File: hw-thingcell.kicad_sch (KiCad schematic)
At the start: 67 parts, among them J1 Conn_01x02_Pin, J2 Conn_Coaxial, J3 SIM8060-6-0-14-00-A, J4 Conn_01x08_Pin, K1 JRC-21F(4100), Q1 PMBT3904235, Q2 PMBT3904235, SW1 SW_Push, U1 ESP32-WROOM-32, U2 SIM800C, U3 NCP1117-3.3_SOT223

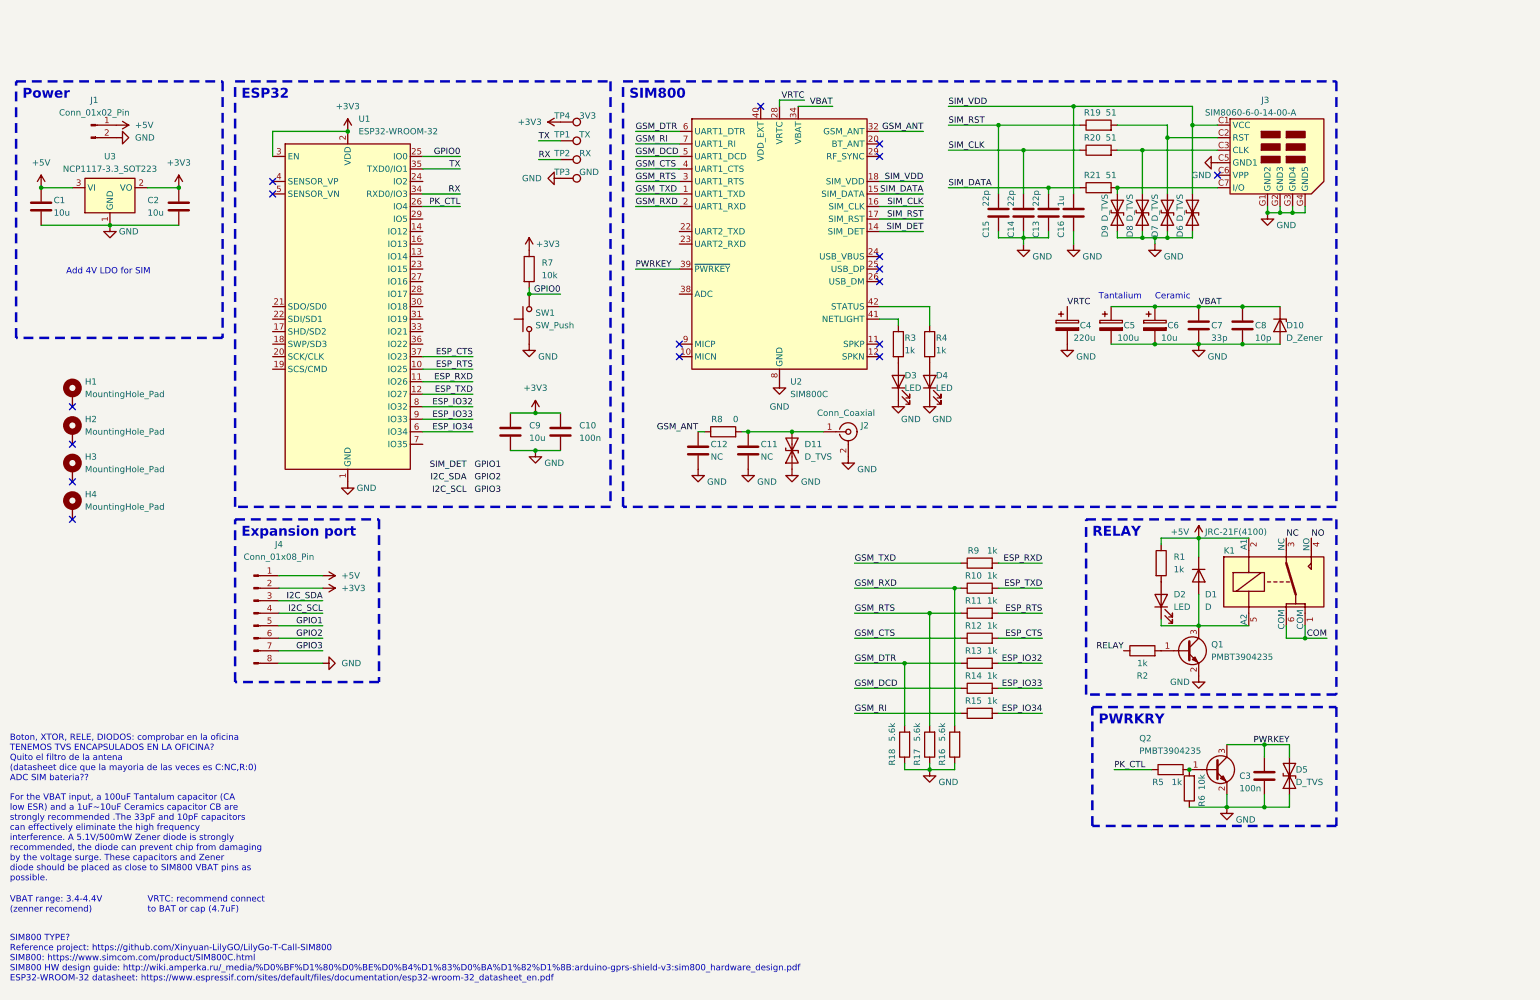
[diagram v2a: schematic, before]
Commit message: Replace SIM800C with SIM868
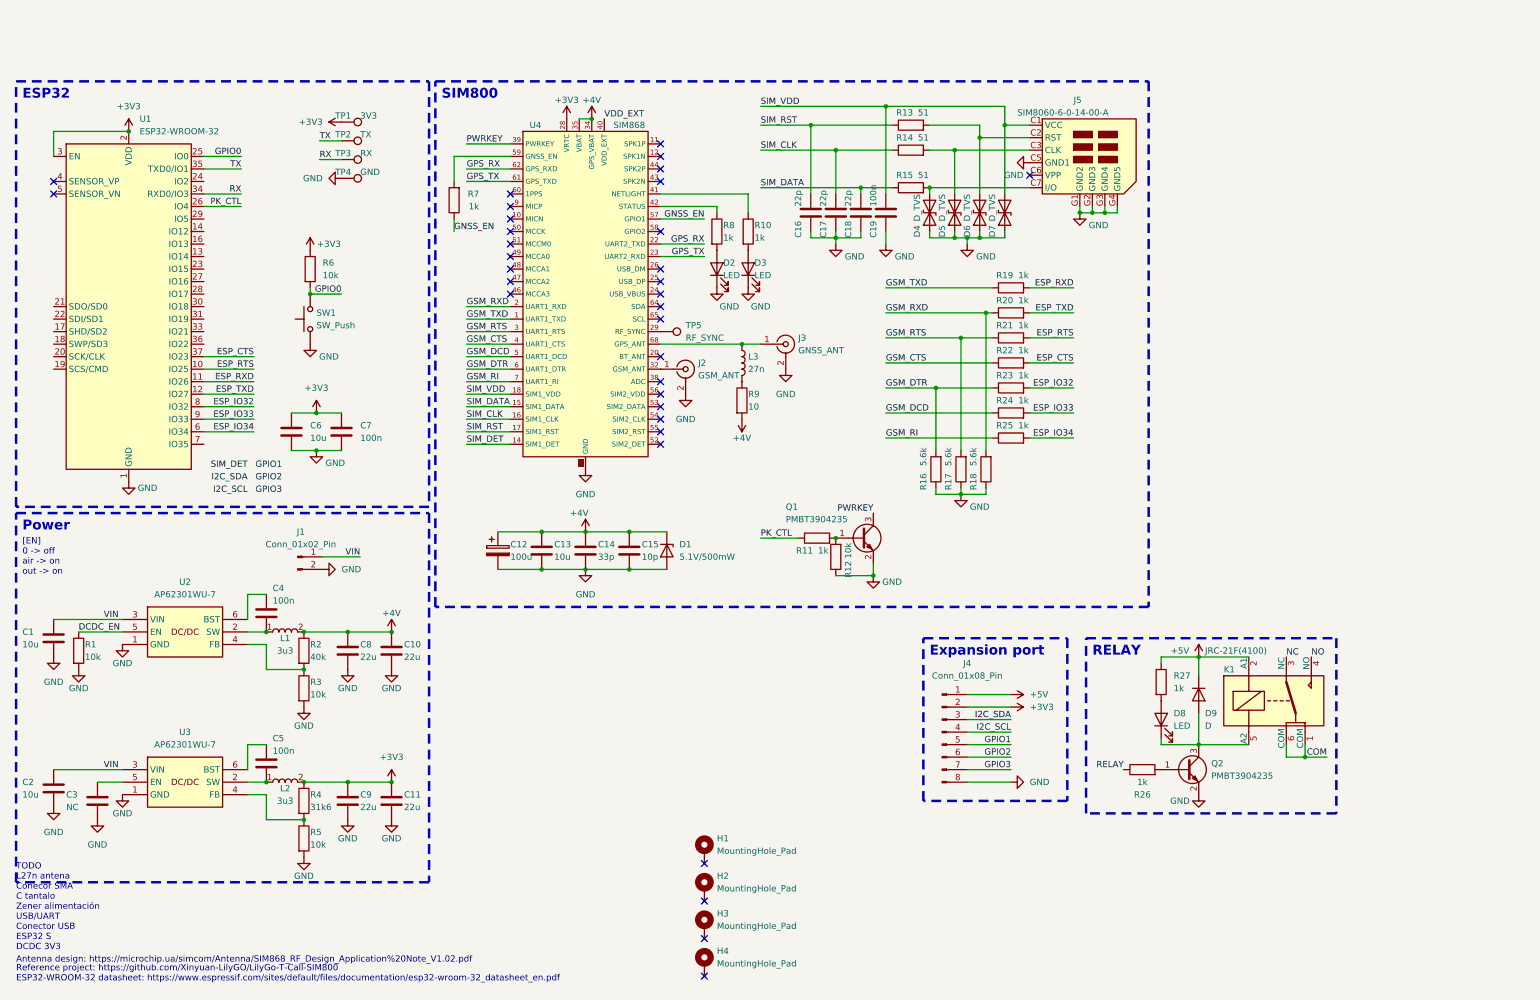
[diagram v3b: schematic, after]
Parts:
- removed C12: NC, Capacitor_SMD:C_0402_1005Metric, symbol Device:C
- removed C4: 220u, symbol Device:C_Polarized
- removed C5: 100u, symbol Device:C_Polarized
- removed C6: 10u, symbol Device:C_Polarized
- removed C7: 33p, Capacitor_SMD:C_0402_1005Metric, symbol Device:C
- removed D10: D_Zener, symbol Device:D_Zener
- removed D11, D5: D_TVS, Diode_SMD:D_0402_1005Metric, symbol Device:D_TVS
- removed D4: LED, LED_SMD:LED_0402_1005Metric, symbol Device:LED
- removed U2: SIM800C, guille-lib:SIM800C, symbol guille-lib:SIM800C
- removed U3: NCP1117-3.3_SOT223, Package_TO_SOT_SMD:SOT-223-3_TabPin2, symbol Regulator_Linear:NCP1117-3.3_SOT223
- added C10, C9: 22u, Capacitor_SMD:C_0805_2012Metric, symbol Device:C
- added C12: 100u, symbol Device:C_Polarized
- added C13: 10u, Capacitor_SMD:C_0805_2012Metric, symbol Device:C
- added C14: 33p, Capacitor_SMD:C_0402_1005Metric, symbol Device:C
- added C15: 10p, Capacitor_SMD:C_0402_1005Metric, symbol Device:C
- added C4, C5: 100n, Capacitor_SMD:C_0402_1005Metric, symbol Device:C
- added D1: 5.1V/500mW, symbol Device:D_Zener
- added D2: LED, LED_SMD:LED_0402_1005Metric, symbol Device:LED
- added J3: GNSS_ANT, symbol Connector:Conn_Coaxial
- added L1, L2: 3u3, guille-lib:SRN5020TA3R3M, symbol guille-lib:SRN5020TA-3R3M
- added L3: 27n, Capacitor_SMD:C_0402_1005Metric, symbol Device:L
- added R1, R5: 10k, Resistor_SMD:R_0402_1005Metric, symbol Device:R
- added R10, R7: 1k, Resistor_SMD:R_0402_1005Metric, symbol Device:R
- added R2: 40k, Resistor_SMD:R_0402_1005Metric, symbol Device:R
- added R9: 10, Resistor_SMD:R_0402_1005Metric, symbol Device:R
- added TP5: RF_SYNC, TestPoint:TestPoint_Pad_D1.0mm, symbol Connector:TestPoint
- added U2, U3: AP62301WU-7, guille-lib:SOT95P280X100-6N, symbol guille-lib:AP62301WU-7
- added U4: SIM868, guille-lib:SIM868, symbol guille-lib:SIM868
- C1, C2: footprint (none) -> Capacitor_SMD:C_0805_2012Metric
- C11: value NC -> 22u; footprint Capacitor_SMD:C_0402_1005Metric -> Capacitor_SMD:C_0805_2012Metric
- C19: renamed from C16; value 1u -> 100n; footprint (none) -> Capacitor_SMD:C_0402_1005Metric
- C3: value 100n -> NC
- C6: renamed from C9; footprint (none) -> Capacitor_SMD:C_0805_2012Metric
- C8: value 10p -> 22u; footprint Capacitor_SMD:C_0402_1005Metric -> Capacitor_SMD:C_0805_2012Metric
- J2: value Conn_Coaxial -> GSM_ANT
- R3: value 1k -> 10k
- R4: value 1k -> 31k6
- R8: value 0 -> 1k
- renumbered C15 to C16, C14 to C17, C13 to C18, C10 to C7, D9 to D4, D8 to D5, D7 to D6, D6 to D7, D2 to D8, D1 to D9, J3 to J5, Q2 to Q1, Q1 to Q2, R5 to R11, R6 to R12, R19 to R13, R20 to R14, R21 to R15, R18 to R16, R16 to R18, R9 to R19, R10 to R20, R11 to R21, R12 to R22, R13 to R23, R14 to R24, R15 to R25, R2 to R26, R1 to R27, R7 to R6, TP4 to TP1, TP1 to TP2, TP2 to TP3, TP3 to TP4
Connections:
- net +3V3: now also C11.1, R4.1, C9.1, L2.2, U4.28 (VRTC); no longer C2.1
- net +5V: no longer C1.1, J1.1 (Pin_1)
- net GND: now also R3.2, C10.2, C12.2, C13.2, C14.2, C15.2, C9.2, D1.2 (A), D2.1 (K), J3.2 (Ext), R1.2, R5.2, U2.1 (GND), U3.1 (GND), U4.13 (GND), U4.19 (GND), U4.21 (GND), U4.27 (GND), U4.30 (GND), U4.31 (GND), U4.33 (GND), U4.36 (GND), U4.37 (GND), U4.45 (GND), U4.63 (GND), U4.66 (GND), U4.67 (GND), U4.69 (GND), U4.70 (GND), U4.71 (GND), U4.72 (GND), U4.73 (GND), U4.74 (GND), U4.75 (GND), U4.76 (GND), U4.77 (GND), U4.8 (GND)
- net GSM_CTS: now also U4.4 (UART1_CTS)
- net GSM_DCD: now also U4.5 (UART1_DCD)
- net GSM_DTR: now also U4.6 (UART1_DTR)
- net GSM_RI: now also U4.7 (UART1_RI)
- net GSM_RTS: now also U4.3 (UART1_RTS)
- net GSM_RXD: now also U4.2 (UART1_RXD)
- net GSM_TXD: now also U4.1 (UART1_TXD)
- net PWRKEY: now also U4.39 (PWRKEY); no longer C3.1
- net SIM_CLK: now also U4.16 (SIM1_CLK)
- net SIM_DATA: now also U4.15 (SIM1_DATA)
- net SIM_DET: now also U4.14 (SIM1_DET)
- net SIM_RST: now also U4.17 (SIM1_RST)
- net SIM_VDD: now also U4.18 (SIM1_VDD)
- net at R4.2: now also R5.1, U3.4 (FB)
- net at R3.1: now also R2.2, U2.4 (FB)
- net at D3.2 (A): now also R10.2; no longer R3.2
- net GSM_ANT: no longer names the net of R8.1
- net GSM_ANT: now also U4.42 (STATUS)
- net VBAT renamed +4V
- net +4V: now also C10.1, C12.1, C13.1, C14.1, C15.1, D1.1 (K), L1.2, R2.1, R9.2, U4.34 (GPS_VBAT), U4.35 (VBAT)
- new net: TP5.1, U4.29 (RF_SYNC)
- new net: D2.2 (A), R8.2
- new net: J2.1 (In), U4.32 (GSM_ANT)
- new net: R10.1, U4.41 (NETLIGHT)
- new net: R7.2, U4.59 (GNSS_EN)
- new net: C3.1, U3.5 (EN)
- new net: J3.1 (In), L3.1, U4.68 (GPS_ANT)
- new net: L3.2, R9.1
- new net: C5.2, L2.1, U3.2 (SW)
- new net: C5.1, U3.6 (BST)
- new net: C4.1, U2.6 (BST)
- new net: C4.2, L1.1, U2.2 (SW)
- new net DCDC_EN: R1.1, U2.5 (EN)
- new net GNSS_EN: R7.1, U4.57 (GPIO1)
- new net GPS_RX: U4.22 (UART2_TXD), U4.62 (GPS_RXD)
- new net GPS_TX: U4.23 (UART2_RXD), U4.61 (GPS_TXD)
- new net VDD_EXT: U4.40 (VDD_EXT)
- new net VIN: C1.1, C2.1, J1.1 (Pin_1), U2.3 (VIN), U3.3 (VIN)
- no-connect marks 17 -> 33
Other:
- note added: "Antenna design: https://microchip.ua/simcom/Antenna/SIM868_RF_Design_Application%20Note_V1.02.pdf"
- note added: "Reference project: https://github.com/Xinyuan-LilyGO/LilyGo-T-Call-SIM800 ESP32-WROOM-32 datasheet: https://www.espressif.com/sites/default/files/documentation/esp32-wroom-32_datasheet_en.pdf"
- note added: "TODO L27n antena Conecor SMA C tantalo Zener alimentación USB/UART Conector USB ESP32 S DCDC 3V3"
- note added: "[EN] 0 -> off air -> on out -> on"
- note removed: "Add 4V LDO for SIM"
- note removed: "Boton, XTOR, RELE, DIODOS: comprobar en la oficina TENEMOS TVS ENCAPSULADOS EN LA OFICINA? Quito el filtro de la antena (datasheet dice que la mayoria de las veces es C:NC,R:0) ADC SIM bateria??"
- note removed: "Ceramic"
- note removed: "For the VBAT input, a 100uF Tantalum capacitor (CA low ESR) and a 1uF~10uF Ceramics capacitor CB are strongly recommended .The 33pF and 10pF capacitors can effectively eliminate the high frequency interference. A 5.1V/500mW Zener diode is strongly recommended, the diode can prevent chip from damaging by the voltage surge. These capacitors and Zener diode should be placed as close to SIM800 VBAT p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"
- note removed: "PWRKRY"
- note removed: "SIM800 TYPE? Reference project: https://github.com/Xinyuan-LilyGO/LilyGo-T-Call-SIM800 SIM800: https://www.simcom.com/product/SIM800C.html SIM800 HW design guide: http://wiki.amperka.ru/_media/%D0%BF%D1%80%D0%BE%D0%B4%D1%83%D0%BA%D1%82%D1%8B:arduino-gprs-shield-v3:sim800_hardware_design.pdf ESP32-WROOM-32 datasheet: https://www.espressif.com/sites/default/files/documentation/esp32-wroom-32_datash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"
- note removed: "Tantalium"
- note removed: "VBAT range: 3.4-4.4V (zenner recomend)"
- note removed: "VRTC: recommend connect to BAT or cap (4.7uF)"
- moved on the sheet: C16, C17, C18, C19, C6, C7, D4, D5, D6, D7, D8, D9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

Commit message: Add antenna connector and passive components
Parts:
- removed C12: 100u, symbol Device:C_Polarized
- removed D1: 5.1V/500mW, symbol Device:D_Zener
- added C?: 100u_tant, guille-lib:CAPPM3528X210N, symbol guille-lib:TPSB107K006R0250
- added D1: BZT52C5V1-7-F, guille-lib:SOD3716X145N, symbol guille-lib:BZT52C5V1-7-F
- J2, J3: footprint (none) -> guille-lib:U.FL_CONNECTOR
- L3: footprint Capacitor_SMD:C_0402_1005Metric -> Inductor_SMD:L_0402_1005Metric; Mouser (none) -> https://www.mouser.es/ProductDetail/Wurth-Elektronik/784780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
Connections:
- net +4V: now also C?.1, D1.1 (K)
- net GND: now also C?.2, D1.2 (A)
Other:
- note added: "TODO USB/UART Conector USB ESP32 S"
- note removed: "TODO L27n antena Conecor SMA C tantalo Zener alimentación USB/UART Conector USB ESP32 S DCDC 3V3"
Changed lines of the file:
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@@
     (stroke (width 0) (type default))
   )
-  (wire (pts (xy 111.76 113.03) (xy 120.65 113.03))
+  (wire (pts (xy 114.3 113.03) (xy 120.65 113.03))
     (stroke (width 0) (type default))
   )
@@
     (stroke (width 0) (type default))
   )
-  (wire (pts (xy 111.76 105.41) (xy 120.65 105.41))
+  (wire (pts (xy 114.3 105.41) (xy 120.65 105.41))
     (stroke (width 0) (type default))
   )
@@
     (effects (font (size 1.27 1.27)) (justify left bottom))
   )
-  (text "TODO\nL27n antena\nConecor SMA\nC tantalo\nZener alimentación\nUSB/UART\nConector USB\nESP32 S\nDCDC 3V3"
-    (at 13.97 190.5 0)
+  (text "TODO\nUSB/UART\nConector USB\nESP32 S" (at 13.97 190.5 0)
     (effects (font (size 1.27 1.27)) (justify left bottom))
   )
@@
     )
   )
-  (symbol (lib_id "Connector:TestPoint") (at 144.78 64.77 270) (unit 1)
-    (in_bom yes) (on_board yes) (dnp no) (fields_autoplaced)
-    (property "Reference" "TP5" (at 149.86 63.5 90)
-      (effects (font (size 1.27 1.27)) (justify left))
+  (symbol (lib_id "guille-lib:TPSB107K006R0250") (at 114.3 109.22 270) (unit 1)
+    (in_bom yes) (on_board yes) (dnp no)
+    (property "Reference" "C?" (at 109.22 109.22 90)
+      (effects (font (size 1.27 1.27)) (justify left top))
     )
-    (property "Value" "RF_SYNC" (at 149.86 66.04 90)
-      (effects (font (size 1.27 1.27)) (justify left))
+    (property "Value" "100u_tant" (at 101.6 106.68 90)
+      (effects (font (size 1.27 1.27)) (justify left top))
     )
-    (property "Footprint" "TestPoint:TestPoint_Pad_D1.0mm" (at 144.78 69.85 0)
-      (effects (font (size 1.27 1.27)) hide)
+    (property "Footprint" "guille-lib:CAPPM3528X210N" (at 18.11 118.11 0)
+      (effects (font (size 1.27 1.27)) (justify left top) hide)
     )
-    (property "Datasheet" "~" (at 144.78 69.85 0)
-      (effects (font (size 1.27 1.27)) hide)
+    (property "Datasheet" "http://datasheets.avx.com/TPS.pdf" (at -81.89 118.11 0)
+      (effects (font (size 1.27 1.27)) (justify left top) hide)
+    )
+    (property "Height" "2.1" (at -281.89 118.11 0)
+      (effects (font (size 1.27 1.27)) (justify left top) hide)
+    )
+    (property "Manufacturer_Name" "AVX" (at -381.89 118.11 0)
+      (effects (font (size 1.27 1.27)) (justify left top) hide)
+    )
+    (property "Manufacturer_Part_Number" "TPSB107K006R0250" (at -481.89 118.11 0)
+      (effects (font (size 1.27 1.27)) (justify left top) hide)
+    )
+    (property "Mouser Part Number" "581-TPSB107K006R0250" (at -581.89 118.11 0)
+      (effects (font (size 1.27 1.27)) (justify left top) hide)
+    )
+    (property "Mouser Price/Stock" "https://www.mouser.co.uk/ProductDetail/AVX/TPSB107K006R0250?qs=im0Xcs1C0VUGGXHMJDxv8A%3D%3D" (at -681.89 118.11 0)
+      (effects (font (size 1.27 1.27)) (justify left top) hide)
     )
     (pin "1")
+    (pin "2")
     (instances
       (project "hw-thingcell"
         (path "/b864757b-52bc-4794-ab53-eb54b6429a77"
-          (reference "TP5") (unit 1)
+          (reference "C?") (unit 1)
         )
       )
     )
   )
-  (symbol (lib_id "Device:D_Zener") (at 146.05 109.22 270) (unit 1)
+  (symbol (lib_id "Connector:TestPoint") (at 144.78 64.77 270) (unit 1)
     (in_bom yes) (on_board yes) (dnp no) (fields_autoplaced)
-    (property "Reference" "D1" (at 148.59 107.95 90)
+    (property "Reference" "TP5" (at 149.86 63.5 90)
       (effects (font (size 1.27 1.27)) (justify left))
     )
-    (property "Value" "5.1V/500mW" (at 148.59 110.49 90)
+    (property "Value" "RF_SYNC" (at 149.86 66.04 90)
       (effects (font (size 1.27 1.27)) (justify left))
     )
-    (property "Footprint" "" (at 146.05 109.22 0)
-      (effects (font (size 1.27 1.27)) hide)
-    )
-    (property "Datasheet" "~" (at 146.05 109.22 0)
+    (property "Footprint" "TestPoint:TestPoint_Pad_D1.0mm" (at 144.78 69.85 0)
       (effects (font (size 1.27 1.27)) hide)
     )
-    (property "Mouser" "https://www.mouser.es/ProductDetail/Diodes-Incorporated/BZT52C5V1-7-F?qs=FFy5bLXC7EennpZVc1%2Fcow%3D%3D" (at 146.05 109.22 90)
+    (property "Datasheet" "~" (at 144.78 69.85 0)
       (effects (font (size 1.27 1.27)) hide)
     )
-    (pin "2")
     (pin "1")
     (instances
       (project "hw-thingcell"
         (path "/b864757b-52bc-4794-ab53-eb54b6429a77"
-          (reference "D1") (unit 1)
+          (reference "TP5") (unit 1)
         )
       )
@@
       (effects (font (size 1.27 1.27)) (justify left))
     )
-    (property "Footprint" "" (at 149.86 72.39 0)
+    (property "Footprint" "guille-lib:U.FL_CONNECTOR" (at 149.86 72.39 0)
       (effects (font (size 1.27 1.27)) hide)
     )
@@
       (effects (font (size 1.27 1.27)) (justify left))
     )
-    (property "Footprint" "Capacitor_SMD:C_0402_1005Metric" (at 161.29 71.12 0)
+    (property "Footprint" "Inductor_SMD:L_0402_1005Metric" (at 161.29 71.12 0)
       (effects (font (size 1.27 1.27)) hide)
     )
@@
       (effects (font (size 1.27 1.27)) hide)
     )
+    (property "Mouser" "https://www.mouser.es/ProductDetail/Wurth-Elektronik/7847804270?qs=QNEnbhJQKvaAR9QxS1FEoQ%3D%3D" (at 161.29 71.12 0)
+      (effects (font (size 1.27 1.27)) hide)
+    )
     (pin "2")
     (pin "1")
@@
       (effects (font (size 1.27 1.27)) (justify left))
     )
-    (property "Footprint" "" (at 170.18 67.31 0)
+    (property "Footprint" "guille-lib:U.FL_CONNECTOR" (at 170.18 67.31 0)
       (effects (font (size 1.27 1.27)) hide)
     )
@@
     )
   )
-  (symbol (lib_id "Device:C_Polarized") (at 111.76 109.22 0) (unit 1)
-    (in_bom yes) (on_board yes) (dnp no)
-    (property "Reference" "C12" (at 114.3 107.95 0)
-      (effects (font (size 1.27 1.27)) (justify left))
-    )
-    (property "Value" "100u" (at 114.3 110.49 0)
-      (effects (font (size 1.27 1.27)) (justify left))
-    )
-    (property "Footprint" "" (at 112.7252 113.03 0)
-      (effects (font (size 1.27 1.27)) hide)
-    )
-    (property "Datasheet" "~" (at 111.76 109.22 0)
-      (effects (font (size 1.27 1.27)) hide)
-    )
-    (property "Note" "Tantalium low ESR" (at 111.76 109.22 0)
-      (effects (font (size 1.27 1.27)) hide)
-    )
-    (property "Mouser" "https://www.mouser.es/ProductDetail/KYOCERA-AVX/TPSB107K006R0250?qs=sGAEpiMZZMtZ1n0r9vR22feWHVMpUcWYCgqJpG32%2Fag%3D" (at 111.76 109.22 0)
-      (effects (font (size 1.27 1.27)) hide)
-    )
-    (pin "1")
-    (pin "2")
-    (instances
-      (project "hw-thingcell"
-        (path "/b864757b-52bc-4794-ab53-eb54b6429a77"
-          (reference "C12") (unit 1)
-        )
-      )
-    )
-  )
   (symbol (lib_id "RF_Module:ESP32-WROOM-32") (at 36.83 59.69 0) (unit 1)
     (in_bom yes) (on_board yes) (dnp no) (fields_autoplaced)
@@
         )
       )
+    )
+  )
+  (symbol (lib_id "guille-lib:BZT52C5V1-7-F") (at 146.05 109.22 270) (unit 1)
+    (in_bom yes) (on_board yes) (dnp no)
+    (property "Reference" "D1" (at 148.59 107.95 90)
+      (effects (font (size 1.27 1.27)) (justify left))
+    )
+    (property "Value" "BZT52C5V1-7-F" (at 148.59 110.49 90)
+      (effects (font (size 1.27 1.27)) (justify left))
+    )
+    (property "Footprint" "guille-lib:SOD3716X145N" (at 48.59 120.65 0)
+      (effects (font (size 1.27 1.27)) (justify left top) hide)
+    )
+    (property "Datasheet" "https://componentsearchengine.com/Datasheets/2/BZT52C5V1-7-F.pdf" (at -51.41 120.65 0)
+      (effects (font (size 1.27 1.27)) (justify left top) hide)
+    )
+    (property "Height" "1.45" (at -251.41 120.65 0)
+      (effects (font (size 1.27 1.27)) (justify left top) hide)
+    )
+    (property "Manufacturer_Name" "Diodes Incorporated" (at -351.41 120.65 0)
+      (effects (font (size 1.27 1.27)) (justify left top) hide)
+    )
+    (property "Manufacturer_Part_Number" "BZT52C5V1-7-F" (at -451.41 120.65 0)
+      (effects (font (size 1.27 1.27)) (justify left top) hide)
+    )
+    (property "Mouser Part Number" "621-BZT52C5V1-F" (at -551.41 120.65 0)
+      (effects (font (size 1.27 1.27)) (justify left top) hide)
+    )
+    (property "Mouser Price/Stock" "https://www.mouser.co.uk/ProductDetail/Diodes-Incorporated/BZT52C5V1-7-F?qs=FFy5bLXC7EennpZVc1%2Fcow%3D%3D" (at -651.41 120.65 0)
+      (effects (font (size 1.27 1.27)) (justify left top) hide)
+    )
+    (property "Note" "5.1V/500mW" (at 146.05 104.14 90)
+      (effects (font (size 1.27 1.27)))
+    )
+    (pin "1")
+    (pin "2")
+    (instances
+      (project "hw-thingcell"
+        (path "/b864757b-52bc-4794-ab53-eb54b6429a77"
+          (reference "D1") (unit 1)
+        )
+      )
